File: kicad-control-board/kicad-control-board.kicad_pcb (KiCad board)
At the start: 2 copper layers, 100 x 110 mm, 99 parts, among them J1 Conn_01x10_Female, J2 Conn_01x15_Male, J3 BA56_3DIG_7SEG, J4 Gate Out, J5 Clock Out, J6 Clock In, J7 Pitch Out, J8 CV Out, J9 Reset In, Q1 2N3904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

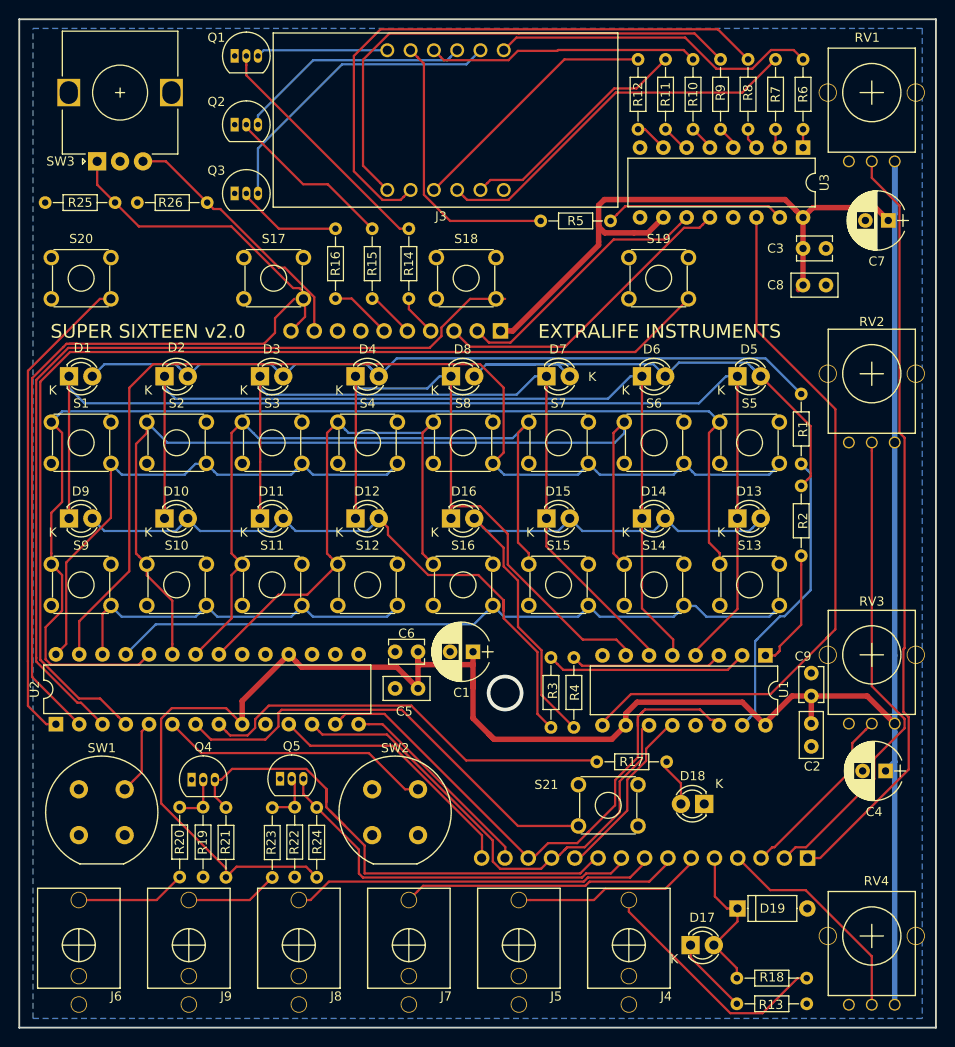
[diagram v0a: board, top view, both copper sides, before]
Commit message: Updating PCB and schematics for assembly bugfixes
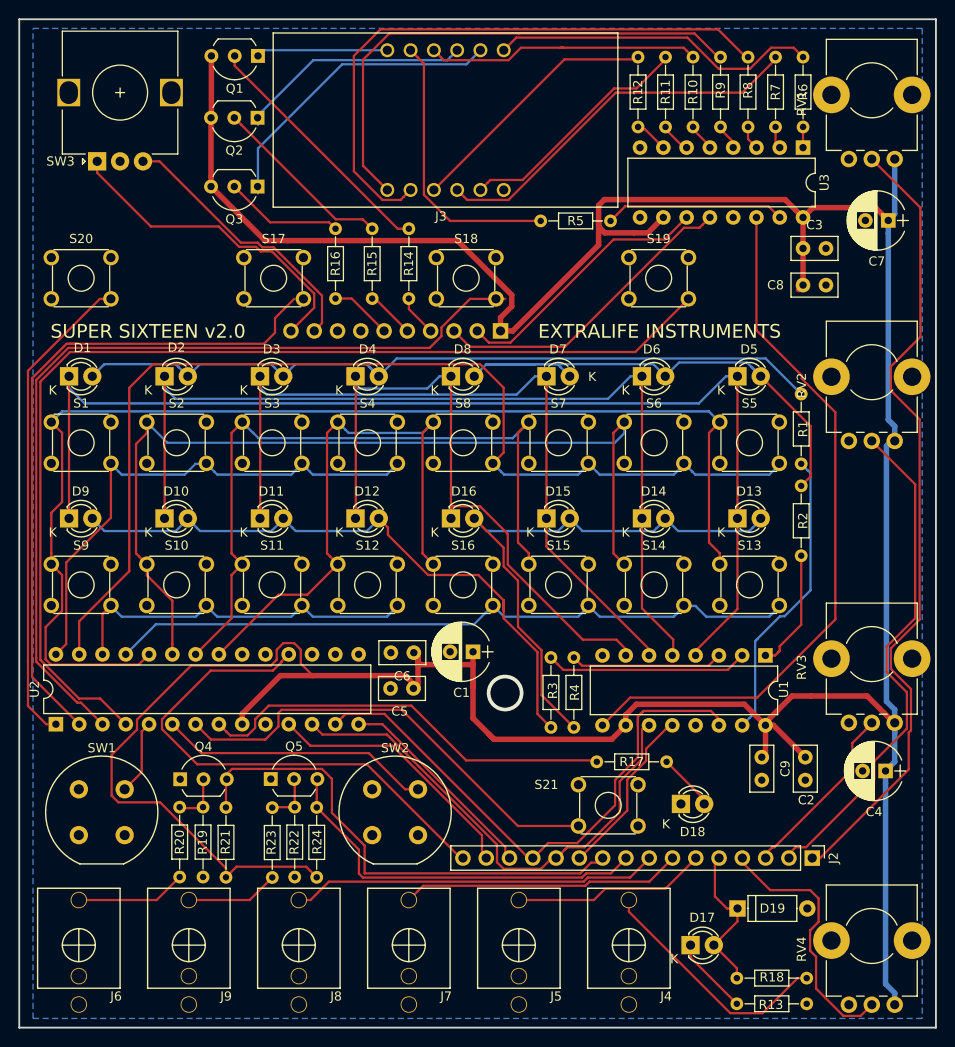
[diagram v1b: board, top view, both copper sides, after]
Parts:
- removed R25, R26: R, Resistors_THT:R_Axial_DIN0204_L3.6mm_D1.6mm_P7.62mm_Horizontal
- C3, C6, C9: footprint Capacitors_THT:C_Disc_D3.8mm_W2.6mm_P2.50mm -> Capacitors_THT:C_Disc_D5.0mm_W2.5mm_P2.50mm
- J2: value Conn_01x15_Male -> Conn_01x16_Male; footprint Pin_Headers:Pin_Header_Straight_1x15_Pitch2.54mm -> Pin_Headers:Pin_Header_Straight_1x16_Pitch2.54mm; moved to F.Cu
- Q1, Q2, Q3: value 2N3904 -> 2N3906; footprint TO_SOT_Packages_THT:TO-92_Inline_Narrow_Oval -> TO_SOT_Packages_THT:TO-92_Inline_Wide
- Q4, Q5: footprint TO_SOT_Packages_THT:TO-92_Inline_Narrow_Oval -> TO_SOT_Packages_THT:TO-92_Inline_Wide
- R17: value R -> 1k
- RV1, RV2, RV3, RV4: footprint Eurocad:Alpha9mmPot -> Potentiometers:Potentiometer_Alps_RK09K_Horizontal
- moved C9 8.59 mm to (93.0, 92.5), turned to 270 degrees
- moved RV4 7.91 mm to (107.5, 119.5), turned to 90 degrees
- moved RV3 7.83 mm to (107.5, 88.8), turned to 90 degrees
- moved RV2 7.75 mm to (107.5, 58.0), turned to 90 degrees
- moved RV1 7.67 mm to (107.5, 27.2), turned to 90 degrees
- moved C2 3.73 mm to (97.8, 92.5)
- moved Q2 2.61 mm to (38.0, 22.8), turned to 180 degrees
- moved Q3 2.61 mm to (38.0, 30.2), turned to 180 degrees
- moved Q1 2.54 mm to (38.0, 16.0), turned to 180 degrees
- moved Q4 1.25 mm to (29.6, 94.9)
- moved Q5 1.01 mm to (39.4, 94.9)
- moved C5 0.50 mm to (55.0, 85.0)
- moved J2 0.50 mm to (98.5, 103.5), turned to 270 degrees
- moved C6 0.47 mm to (55.0, 81.1)
- moved R10 0.25 mm to (85.5, 23.8)
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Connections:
- J3 pad 6: Net-(J3-Pad6) -> (no net)
- J4 pad 2: Net-(J4-Pad2) -> (no net)
- J5 pad 2: Net-(J5-Pad2) -> (no net)
- J6 pad 2: Net-(J6-Pad2) -> (no net)
- J7 pad 2: Net-(J7-Pad2) -> (no net)
- J8 pad 2: Net-(J8-Pad2) -> (no net)
- J9 pad 2: Net-(J9-Pad2) -> (no net)
- Q1 pad 1: GND -> Net-(J3-Pad12)
- Q1 pad 3: Net-(J3-Pad12) -> +5V
- Q2 pad 1: GND -> Net-(J3-Pad9)
- Q2 pad 3: Net-(J3-Pad9) -> +5V
- Q3 pad 1: GND -> Net-(J3-Pad8)
- Q3 pad 3: Net-(J3-Pad8) -> +5V
- S1 pad 2: Net-(S1-Pad2) -> (no net)
- S1 pad 3: Net-(S1-Pad3) -> (no net)
- S10 pad 2: Net-(S10-Pad2) -> (no net)
- S10 pad 3: Net-(S10-Pad3) -> (no net)
- S11 pad 2: Net-(S11-Pad2) -> (no net)
- S11 pad 3: Net-(S11-Pad3) -> (no net)
- S12 pad 2: Net-(S12-Pad2) -> (no net)
- S12 pad 3: Net-(S12-Pad3) -> (no net)
- S13 pad 2: Net-(S13-Pad2) -> (no net)
- S13 pad 3: Net-(S13-Pad3) -> (no net)
- S14 pad 2: Net-(S14-Pad2) -> (no net)
- S14 pad 3: Net-(S14-Pad3) -> (no net)
- S15 pad 2: Net-(S15-Pad2) -> (no net)
- S15 pad 3: Net-(S15-Pad3) -> (no net)
- S16 pad 2: Net-(S16-Pad2) -> (no net)
- S16 pad 3: Net-(S16-Pad3) -> (no net)
- S17 pad 1: Net-(S17-Pad1) -> (no net)
- S17 pad 3: Net-(S17-Pad3) -> (no net)
- S18 pad 1: Net-(S18-Pad1) -> (no net)
- S18 pad 3: Net-(S18-Pad3) -> (no net)
- S19 pad 1: Net-(S19-Pad1) -> (no net)
- S19 pad 3: Net-(S19-Pad3) -> (no net)
- S2 pad 2: Net-(S2-Pad2) -> (no net)
- S2 pad 3: Net-(S2-Pad3) -> (no net)
- S20 pad 1: Net-(S20-Pad1) -> (no net)
- S20 pad 3: Net-(S20-Pad3) -> (no net)
- S21 pad 1: Net-(S21-Pad1) -> (no net)
- S21 pad 3: Net-(S21-Pad3) -> (no net)
- S3 pad 2: Net-(S3-Pad2) -> (no net)
- S3 pad 3: Net-(S3-Pad3) -> (no net)
- S4 pad 2: Net-(S4-Pad2) -> (no net)
- S4 pad 3: Net-(S4-Pad3) -> (no net)
- S5 pad 2: Net-(S5-Pad2) -> (no net)
- S5 pad 3: Net-(S5-Pad3) -> (no net)
- S6 pad 2: Net-(S6-Pad2) -> (no net)
- S6 pad 3: Net-(S6-Pad3) -> (no net)
- S7 pad 2: Net-(S7-Pad2) -> (no net)
- S7 pad 3: Net-(S7-Pad3) -> (no net)
- S8 pad 2: Net-(S8-Pad2) -> (no net)
- S8 pad 3: Net-(S8-Pad3) -> (no net)
- S9 pad 2: Net-(S9-Pad2) -> (no net)
- S9 pad 3: Net-(S9-Pad3) -> (no net)
- U2 pad 18: +5V -> SPI_Reset
- U2 pad 19: Net-(U2-Pad19) -> (no net)
- U2 pad 20: Net-(U2-Pad20) -> (no net)
- U3 pad 9: Net-(U3-Pad9) -> (no net)
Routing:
- net +5V: track 311.5 -> 386.6 mm
- net SPI_Reset: track 0.00 -> 56.3 mm
- net AD1: track 83.1 -> 88.7 mm
- net AD4: track 24.3 -> 28.9 mm
- net ClockIn: track 57.8 -> 53.9 mm
- net AD2: track 52.9 -> 55.9 mm
- net Net-(Q3-Pad2): track 11.5 -> 12.9 mm
- net Net-(Q2-Pad2): track 18.6 -> 20.1 mm
- net ENC2: track 28.5 -> 29.8 mm
- net Net-(D18-Pad2): track 5.15 -> 6.30 mm
- net Net-(U1-Pad9): track 78.4 -> 77.6 mm
- net Net-(Q1-Pad2): track 26.8 -> 27.4 mm
- net ENC1: track 34.8 -> 35.5 mm
- net ResetIn: track 42.4 -> 41.8 mm

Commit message: Swapping in 660R resistors
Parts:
- R14, R15, R16: value 1K -> 660
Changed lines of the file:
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@@
     (add_net "Net-(J3-Pad4)")
     (add_net "Net-(J3-Pad5)")
+    (add_net "Net-(J3-Pad6)")
     (add_net "Net-(J3-Pad7)")
     (add_net "Net-(J3-Pad8)")
     (add_net "Net-(J3-Pad9)")
+    (add_net "Net-(J4-Pad2)")
     (add_net "Net-(J4-Pad3)")
+    (add_net "Net-(J5-Pad2)")
+    (add_net "Net-(J6-Pad2)")
     (add_net "Net-(J6-Pad3)")
+    (add_net "Net-(J7-Pad2)")
+    (add_net "Net-(J8-Pad2)")
+    (add_net "Net-(J9-Pad2)")
     (add_net "Net-(J9-Pad3)")
     (add_net "Net-(Q1-Pad2)")
@@
     (add_net "Net-(R9-Pad1)")
     (add_net "Net-(S1-Pad1)")
+    (add_net "Net-(S1-Pad2)")
+    (add_net "Net-(S1-Pad3)")
     (add_net "Net-(S1-Pad4)")
     (add_net "Net-(S10-Pad1)")
+    (add_net "Net-(S10-Pad2)")
+    (add_net "Net-(S10-Pad3)")
     (add_net "Net-(S10-Pad4)")
     (add_net "Net-(S11-Pad1)")
+    (add_net "Net-(S11-Pad2)")
+    (add_net "Net-(S11-Pad3)")
     (add_net "Net-(S12-Pad1)")
+    (add_net "Net-(S12-Pad2)")
+    (add_net "Net-(S12-Pad3)")
+    (add_net "Net-(S13-Pad2)")
+    (add_net "Net-(S13-Pad3)")
     (add_net "Net-(S13-Pad4)")
+    (add_net "Net-(S14-Pad2)")
+    (add_net "Net-(S14-Pad3)")
+    (add_net "Net-(S15-Pad2)")
+    (add_net "Net-(S15-Pad3)")
+    (add_net "Net-(S16-Pad2)")
+    (add_net "Net-(S16-Pad3)")
+    (add_net "Net-(S17-Pad1)")
+    (add_net "Net-(S17-Pad3)")
+    (add_net "Net-(S18-Pad1)")
+    (add_net "Net-(S18-Pad3)")
+    (add_net "Net-(S19-Pad1)")
+    (add_net "Net-(S19-Pad3)")
+    (add_net "Net-(S2-Pad2)")
+    (add_net "Net-(S2-Pad3)")
+    (add_net "Net-(S20-Pad1)")
+    (add_net "Net-(S20-Pad3)")
+    (add_net "Net-(S21-Pad1)")
+    (add_net "Net-(S21-Pad3)")
+    (add_net "Net-(S3-Pad2)")
+    (add_net "Net-(S3-Pad3)")
+    (add_net "Net-(S4-Pad2)")
+    (add_net "Net-(S4-Pad3)")
+    (add_net "Net-(S5-Pad2)")
+    (add_net "Net-(S5-Pad3)")
     (add_net "Net-(S5-Pad4)")
+    (add_net "Net-(S6-Pad2)")
+    (add_net "Net-(S6-Pad3)")
+    (add_net "Net-(S7-Pad2)")
+    (add_net "Net-(S7-Pad3)")
+    (add_net "Net-(S8-Pad2)")
+    (add_net "Net-(S8-Pad3)")
+    (add_net "Net-(S9-Pad2)")
+    (add_net "Net-(S9-Pad3)")
     (add_net "Net-(U1-Pad9)")
+    (add_net "Net-(U2-Pad19)")
+    (add_net "Net-(U2-Pad20)")
+    (add_net "Net-(U3-Pad9)")
     (add_net Pitch)
     (add_net ResetIn)
@@
       (effects (font (size 1 1) (thickness 0.15)))
     )
-    (fp_text value 1K (at 3.81 1.86 270) (layer F.Fab)
+    (fp_text value 660 (at 3.81 1.86 270) (layer F.Fab)
       (effects (font (size 1 1) (thickness 0.15)))
     )
@@
       (effects (font (size 1 1) (thickness 0.15)))
     )
-    (fp_text value 1K (at 3.81 1.86 270) (layer F.Fab)
+    (fp_text value 660 (at 3.81 1.86 270) (layer F.Fab)
       (effects (font (size 1 1) (thickness 0.15)))
     )
@@
       (effects (font (size 1 1) (thickness 0.15)))
     )
-    (fp_text value 1K (at 3.81 1.86 270) (layer F.Fab)
-      (effects (font (size 1 1) (thickness 0.15)))
-    )
+    (fp_text value 660 (at 3.81 1.86 270) (layer F.Fab)
+      (effects (font (size 1 1) (thickness 0.15)))
+    )
